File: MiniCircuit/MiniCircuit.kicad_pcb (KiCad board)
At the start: 2 copper layers, 88.8 x 73.9 mm, 32 parts, among them IC1 MAX4737EUD+, IC2 MAX4737EUD+, IC3 MAX4737EUD+, IC4 MAX4737EUD+, J1 Conn_02x16_Odd_Even, J2 Conn_01x08, SW1 SW_DIP_x08, U1 LM6172, U2 OPA2277, U3 MCP3008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

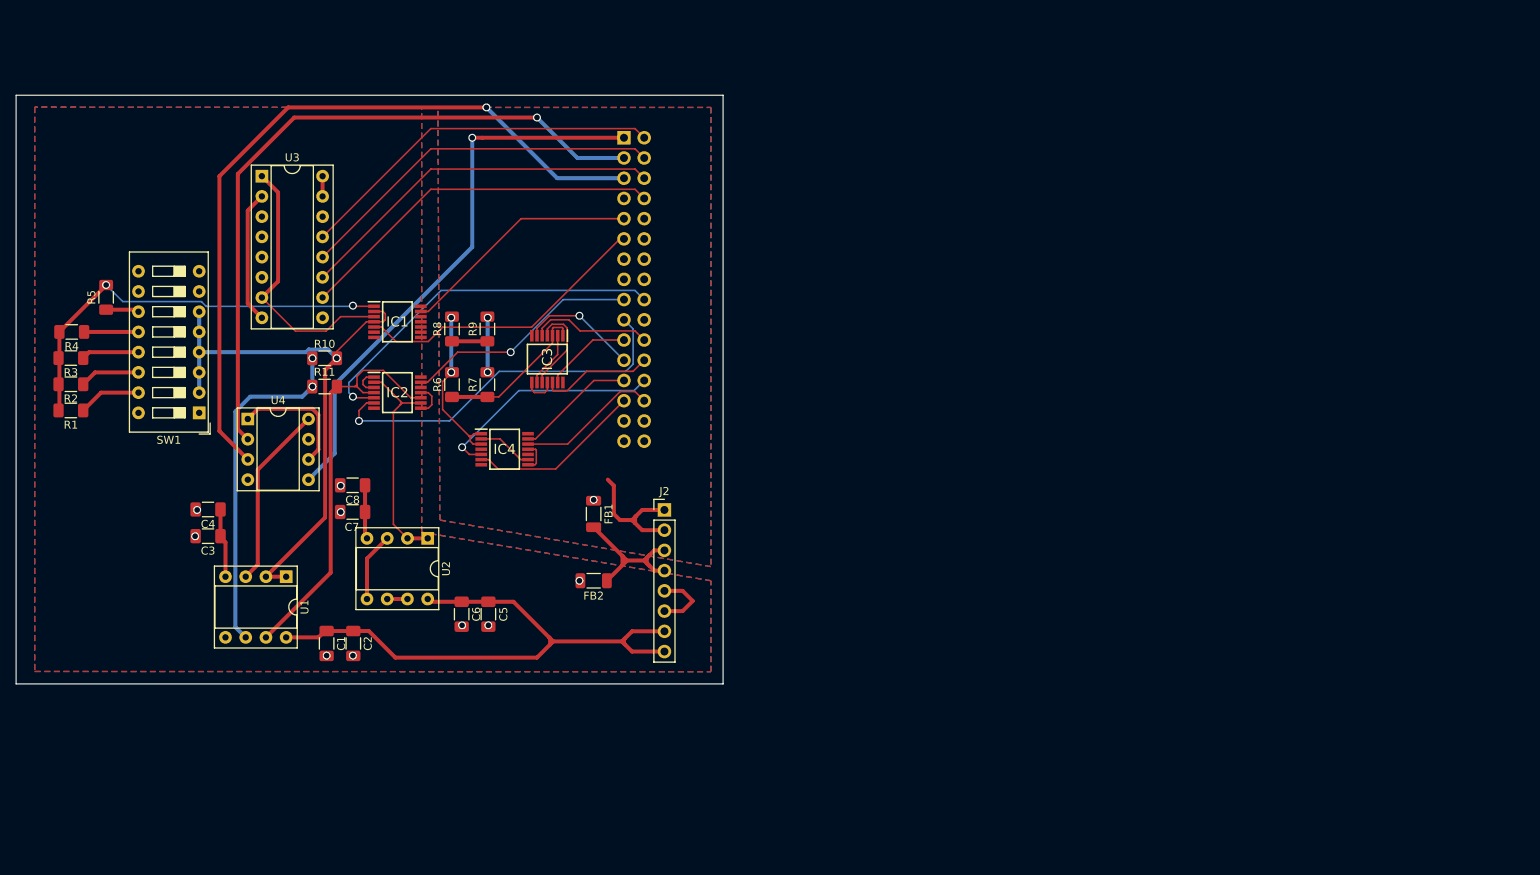
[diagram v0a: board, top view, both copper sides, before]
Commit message: Everything done except routing of digital signals and adding Vias
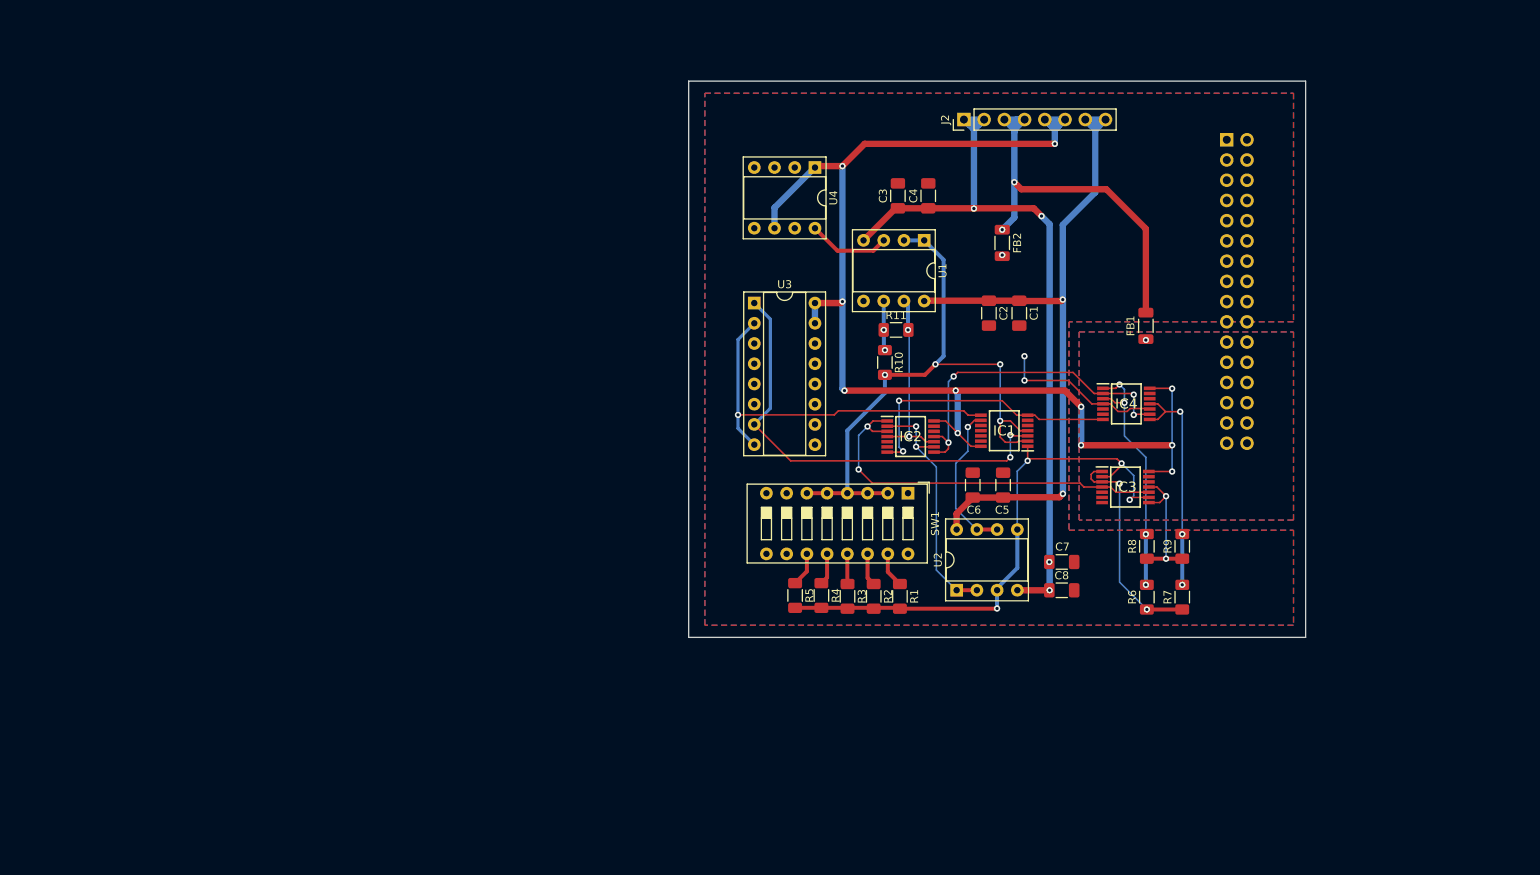
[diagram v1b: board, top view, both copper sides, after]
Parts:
- moved R1 106.7 mm to (161.7, 87.1), turned to -90 degrees
- moved R2 104.3 mm to (158.4, 87.1), turned to -90 degrees
- moved R3 102.0 mm to (155.1, 87.1), turned to -90 degrees
- moved R4 99.8 mm to (151.8, 86.9), turned to -90 degrees
- moved C4 98.6 mm to (165.2, 36.8), turned to 90 degrees
- moved C3 96.6 mm to (161.4, 36.8), turned to 90 degrees
- moved C1 96.4 mm to (176.6, 51.5)
- moved R5 94.3 mm to (148.5, 86.9), turned to -90 degrees
- moved R9 91.4 mm to (197.1, 80.8)
- moved R8 91.4 mm to (192.7, 80.8)
- moved R7 91.2 mm to (197.1, 87.1)
- moved R6 91.2 mm to (192.7, 87.1)
- moved U1 90.6 mm to (164.7, 42.3)
- moved C8 90.0 mm to (182.0, 86.3), turned to 0 degrees
- moved C2 89.9 mm to (172.8, 51.5)
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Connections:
- net /S1in renamed /Driver_FB
- net Net-(U1A-+) renamed /DAC_output
- net Net-(U1B--) renamed /Write_FB
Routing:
- net /+5V: track 26.5 -> 161.1 mm, vias 0 -> 11
- net /SCK: track 95.1 -> 0.00 mm, vias 1 -> 0
- net /DAC_CSbar: track 87.4 -> 0.00 mm, vias 1 -> 0
- net /LDACbar: track 70.5 -> 0.00 mm, vias 1 -> 0
- net /-15V: track 33.3 -> 93.9 mm, vias 0 -> 4
- net /Control10A: track 47.3 -> 0.00 mm, vias 1 -> 0
- net /Control9B: track 47.0 -> 0.00 mm, vias 1 -> 0
- net /Dout: track 46.5 -> 0.00 mm
- net /Din: track 46.5 -> 0.00 mm
- net /ADC_CSbar: track 46.5 -> 0.00 mm
- net /CLK: track 46.5 -> 0.00 mm
- net /Control7: track 37.5 -> 0.00 mm
- net /Write_FB: track 43.4 -> 6.23 mm
- net GNDD: track 0.00 -> 35.2 mm, vias 1 -> 3
- net /S9out: track 15.5 -> 49.0 mm, vias 0 -> 2
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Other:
- board size 88.8 x 73.9 mm -> 77.5 x 69.8 mm

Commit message: Changed Schematic to include CD4066 instead of MAX4737. Design Constraints, Routing and Layout remaining
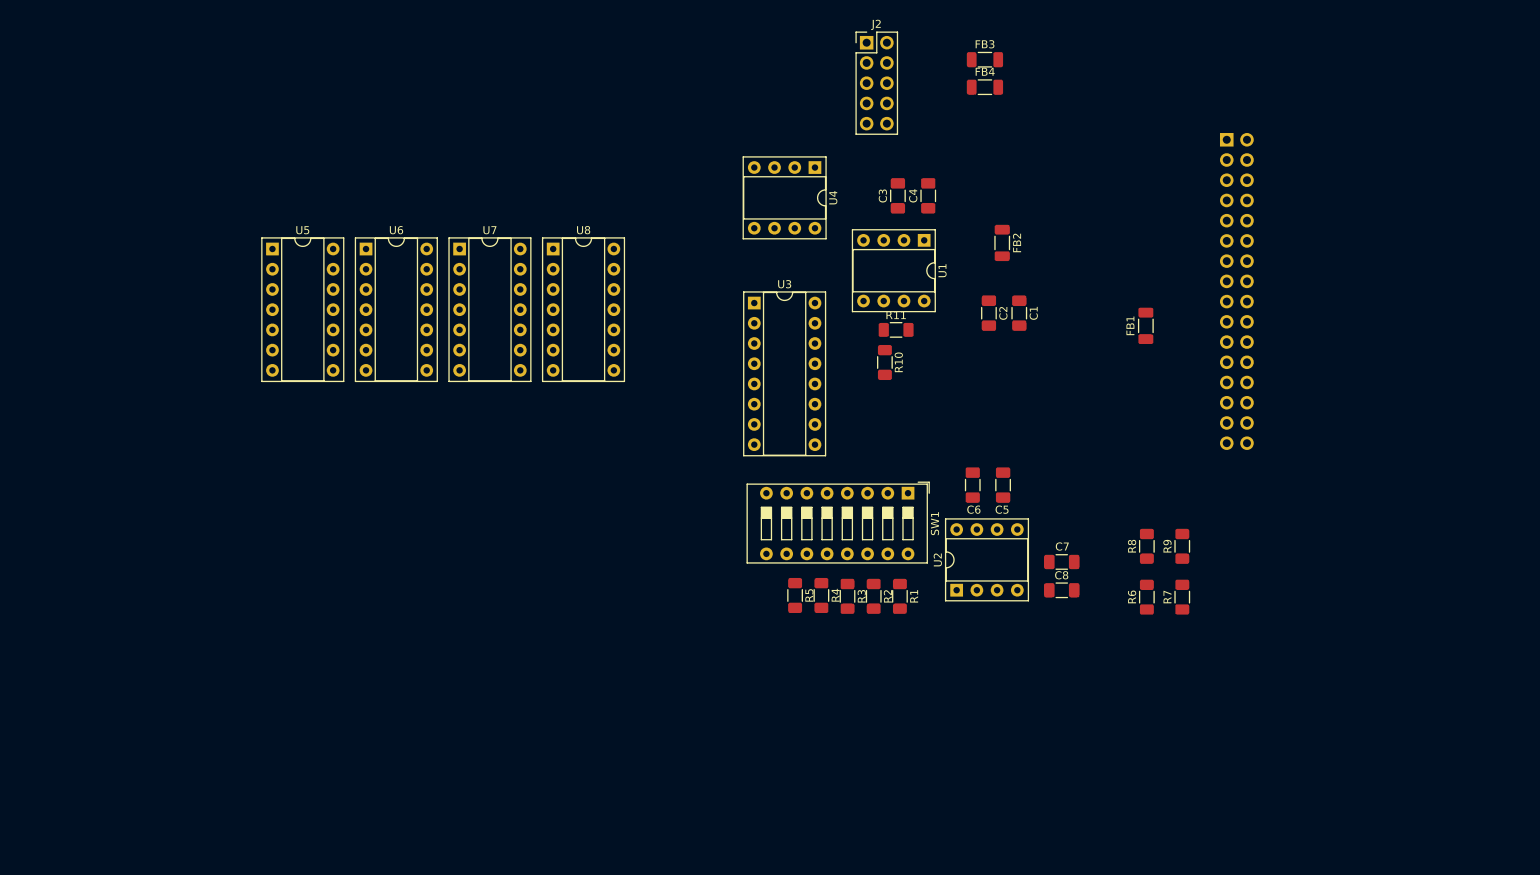
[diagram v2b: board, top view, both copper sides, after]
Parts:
- removed IC1, IC2, IC3, IC4: MAX4737EUD+, MAX4737:SOP65P640X110-14N
- added FB3: FerriteBead, Inductor_SMD:L_1206_3216Metric_Pad1.22x1.90mm_HandSolder, F.Cu at (172.3, 19.7)
- added FB4: FerriteBead, Inductor_SMD:L_1206_3216Metric_Pad1.22x1.90mm_HandSolder, F.Cu at (172.3, 23.1)
- added U5: CD4066BE, Package_DIP:DIP-14_W7.62mm_Socket, F.Cu at (82.9, 43.4)
- added U6: CD4066BE, Package_DIP:DIP-14_W7.62mm_Socket, F.Cu at (94.6, 43.4)
- added U7: CD4066BE, Package_DIP:DIP-14_W7.62mm_Socket, F.Cu at (106.4, 43.4)
- added U8: CD4066BE, Package_DIP:DIP-14_W7.62mm_Socket, F.Cu at (118.1, 43.4)
- J2: value Conn_01x08 -> Conn_02x05_Top_Bottom; footprint Connector_PinHeader_2.54mm:PinHeader_1x08_P2.54mm_Vertical -> Connector_PinHeader_2.54mm:PinHeader_2x05_P2.54mm_Vertical
- moved J2 15.6 mm to (157.5, 17.5), turned to 0 degrees
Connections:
- J2 pad 1: /-15V -> /+15V
- J2 pad 2: /-15V -> /-5V
- J2 pad 3: /PowerGND -> /-5V
- J2 pad 5: /+5V -> /-15V
- J2 pad 6: /+5V -> /+15V
- J2 pad 7: /+15V -> /+5V
- J2 pad 8: /+15V -> /+5V
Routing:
- net /+5V: track 161.1 -> 0.00 mm, vias 11 -> 0
- net /-15V: track 93.9 -> 0.00 mm, vias 4 -> 0
- net /+15V: track 89.5 -> 0.00 mm, vias 2 -> 0
- net /Driver_FB: track 78.4 -> 0.00 mm, vias 4 -> 0
- net /Driver_op: track 70.8 -> 0.00 mm, vias 4 -> 0
- net /S7out: track 56.2 -> 0.00 mm, vias 2 -> 0
- net /PowerGND: track 50.4 -> 0.00 mm, vias 2 -> 0
- net /S9out: track 49.0 -> 0.00 mm, vias 2 -> 0
- net /S8out: track 47.9 -> 0.00 mm, vias 1 -> 0
- net /S10out: track 42.0 -> 0.00 mm, vias 4 -> 0
- net GNDD: track 35.2 -> 0.00 mm, vias 3 -> 0
- net /Vt1: track 31.7 -> 0.00 mm, vias 4 -> 0
- net /S10inA: track 31.1 -> 0.00 mm, vias 2 -> 0
- net /Vt2: track 28.5 -> 0.00 mm, vias 3 -> 0
- net /Hz1: track 27.6 -> 0.00 mm, vias 2 -> 0
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- removed copper zone on B.Cu, net GNDA
- removed copper zone on F.Cu, net GNDA
- removed copper zone on B.Cu, net GNDD
- removed copper zone on F.Cu, net GNDD
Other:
- board outline removed

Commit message: PCB Done, only final touch and verification necessary
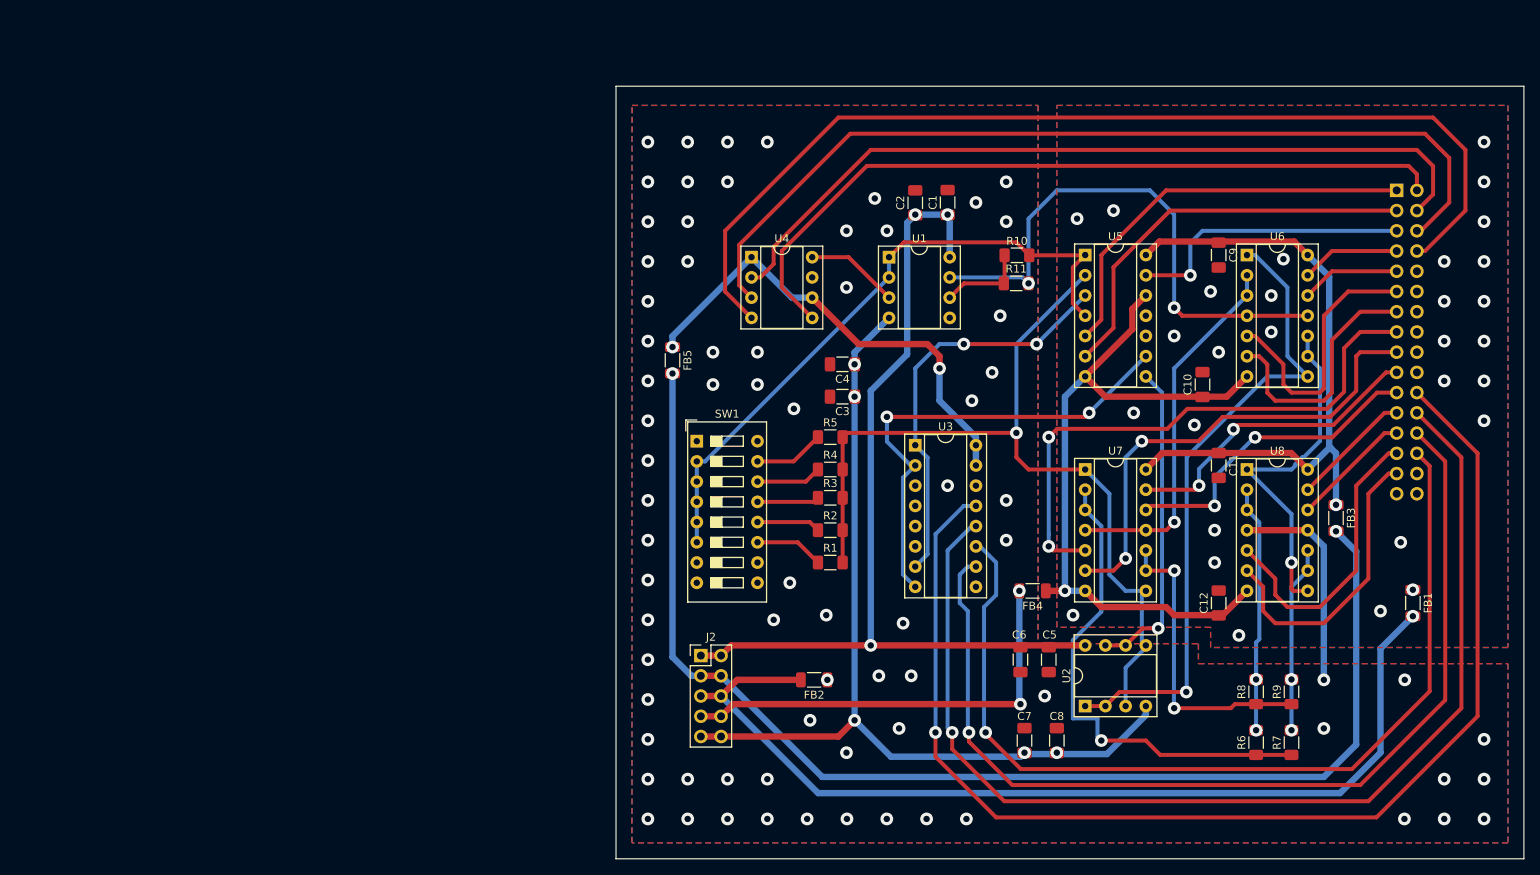
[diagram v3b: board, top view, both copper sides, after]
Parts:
- added C10: 0.1uF, Capacitor_SMD:C_1206_3216Metric_Pad1.33x1.80mm_HandSolder, F.Cu at (199.6, 60.5)
- added C11: 0.1uF, Capacitor_SMD:C_1206_3216Metric_Pad1.33x1.80mm_HandSolder, F.Cu at (201.7, 70.6)
- added C12: 0.1uF, Capacitor_SMD:C_1206_3216Metric_Pad1.33x1.80mm_HandSolder, F.Cu at (201.7, 87.9)
- added C9: 0.1uF, Capacitor_SMD:C_1206_3216Metric_Pad1.33x1.80mm_HandSolder, F.Cu at (201.7, 44.2)
- added FB5: FerriteBead, Inductor_SMD:L_1206_3216Metric_Pad1.22x1.90mm_HandSolder, F.Cu at (133.1, 57.4)
- J2: value Conn_02x05_Top_Bottom -> Conn_02x05_Odd_Even
- moved U6 110.6 mm to (205.2, 44.2)
- moved U5 102.1 mm to (184.9, 44.2)
- moved U8 91.4 mm to (205.2, 71.1)
- moved U7 83.3 mm to (184.9, 71.1)
- moved J2 79.7 mm to (136.7, 94.5)
- moved FB3 72.5 mm to (216.4, 77.2), turned to -90 degrees
- moved FB4 63.5 mm to (178.3, 86.4), turned to 180 degrees
- moved FB2 59.7 mm to (150.9, 97.5), turned to 180 degrees
- moved FB1 48.3 mm to (226.1, 87.9), turned to -90 degrees
- moved SW1 27.3 mm to (136.1, 67.6), turned to 0 degrees
- moved U3 27.0 mm to (163.6, 68.1)
- moved C3 26.2 mm to (154.4, 62.0), turned to 180 degrees
- moved C4 23.7 mm to (154.4, 57.9), turned to 180 degrees
- moved C7 22.9 mm to (177.3, 105.2), turned to 90 degrees
- moved R6 22.8 mm to (206.4, 105.4)
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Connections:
- J1 pad 1: /LDACbar -> /Control7
- J1 pad 11: /Control7 -> /Control9B
- J1 pad 13: /Control8 -> /Control10A
- J1 pad 15: unconnected-(J1-Pin_15-Pad15) -> /ControlAF_1B
- J1 pad 17: /Control9A -> /ControlAF_2A
- J1 pad 18: /Control9B -> unconnected-(J1-Pin_18-Pad18)
- J1 pad 19: /Control10A -> /ControlAF_1A
- J1 pad 2: /CLK -> /LDACbar
- J1 pad 20: /Control10B -> unconnected-(J1-Pin_20-Pad20)
- J1 pad 21: /ControlAF_1A -> /ControlAF_2B
- J1 pad 22: /ControlAF_1B -> /CLK
- J1 pad 23: /ControlAF_2A -> /ControlAF_3A
- J1 pad 24: /ControlAF_2B -> /Dout
- J1 pad 25: /ControlAF_3A -> /ControlAF_4B
- J1 pad 26: /ControlAF_3B -> /ADC_CSbar
- J1 pad 27: /ControlAF_4A -> /ControlAF_3B
- J1 pad 28: /ControlAF_4B -> /Din
- J1 pad 29: unconnected-(J1-Pin_29-Pad29) -> /ControlAF_4A
- J1 pad 3: /DAC_CSbar -> /Control8
- J1 pad 4: /Dout -> /DAC_CSbar
- J1 pad 5: /SCK -> /Control1
- J1 pad 6: /Din -> /SCK
- J1 pad 7: /SDI -> /Control9A
- J1 pad 8: /ADC_CSbar -> /SDI
- J1 pad 9: /Control1 -> /Control10B
- J2 pad 2: /-5V -> /+15V
- J2 pad 3: /-5V -> /+5V
- J2 pad 4: /PowerGND -> /+5V
- J2 pad 5: /-15V -> /PowerGND
- J2 pad 6: /+15V -> /PowerGND
- J2 pad 7: /+5V -> /-5V
- J2 pad 8: /+5V -> /-5V
- J2 pad 9: /PowerGND -> /-15V
- SW1 pad 11: /S6out -> /S2out
- SW1 pad 12: /S5out -> /S3out
- SW1 pad 14: /S3out -> /S5out
- SW1 pad 15: /S2out -> /S6out
- U3 pad 15: /+5V -> /+5VA
- U3 pad 16: /+5V -> /+5VA
- U4 pad 1: /+5V -> /+5VA
- U4 pad 6: /+5V -> /+5VA
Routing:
- net /+5V: track 0.00 -> 157.2 mm, vias 0 -> 2
- net /CLK: track 0.00 -> 154.8 mm, vias 0 -> 1
- net /Dout: track 0.00 -> 140.9 mm, vias 0 -> 1
- net /SDI: track 0.00 -> 128.7 mm
- net /ADC_CSbar: track 0.00 -> 125.4 mm, vias 0 -> 1
- net /PowerGND: track 0.00 -> 122.2 mm, vias 0 -> 1
- net /Din: track 0.00 -> 117.8 mm, vias 0 -> 1
- net /+15V: track 0.00 -> 114.7 mm, vias 0 -> 3
- net /SCK: track 0.00 -> 114.6 mm
- net /-15V: track 0.00 -> 114.5 mm, vias 0 -> 5
- net /Driver_op: track 0.00 -> 109.3 mm, vias 0 -> 1
- net /DAC_CSbar: track 0.00 -> 100.7 mm
- net /LDACbar: track 0.00 -> 96.6 mm
- net /-5VD: track 0.00 -> 91.5 mm, vias 0 -> 1
- net /Driver_FB: track 0.00 -> 81.4 mm
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- added copper zone on B.Cu, net GNDA
- added copper zone on F.Cu, net GNDA
- added copper zone on B.Cu, net GNDD
- added copper zone on F.Cu, net GNDD
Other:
- board outline added: 114 x 97 mm

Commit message: All errors and warnings rectified. Silkscreen contents added.
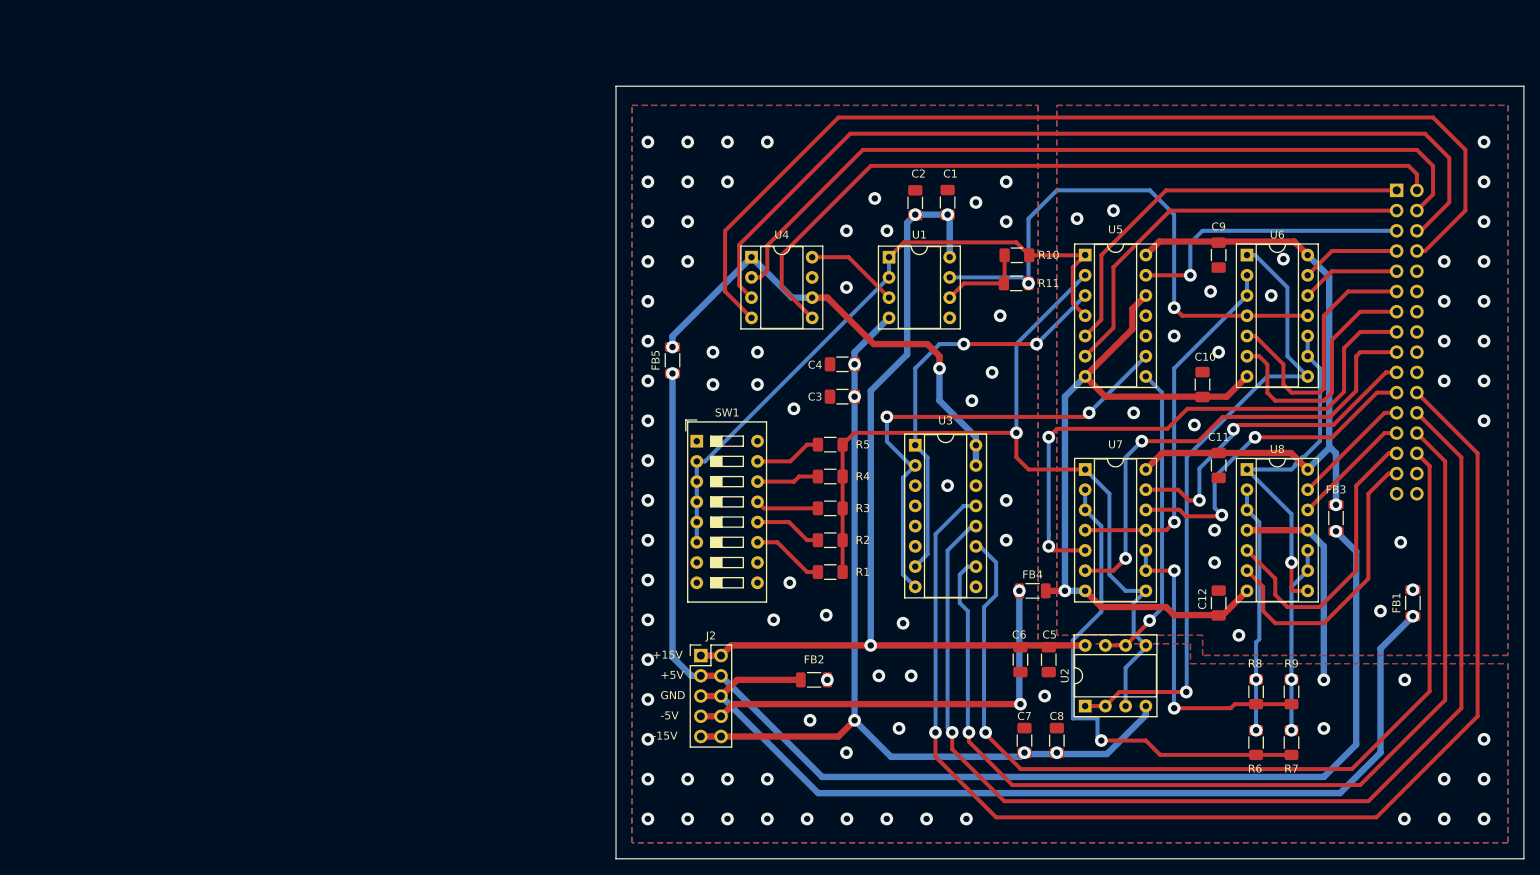
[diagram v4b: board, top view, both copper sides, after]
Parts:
- moved R3 1.32 mm to (152.9, 76.0)
- moved R2 1.26 mm to (152.9, 80.0)
- moved R1 1.20 mm to (152.9, 84.0)
- moved R5 0.94 mm to (152.9, 68.0)
- moved R4 0.88 mm to (152.9, 72.0)
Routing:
- net /Vt1: track 34.6 -> 31.0 mm
- net /ControlAF_2B: track 39.7 -> 42.4 mm
- net /ControlAF_1A: track 39.2 -> 41.4 mm
- net /Driver_op: track 109.3 -> 110.8 mm
- net /S8in: track 40.2 -> 39.1 mm
- net /DAC_CSbar: track 100.7 -> 101.3 mm
- net /S3out: track 8.01 -> 8.54 mm
- net GNDD: vias 28 -> 27
- net (no net): vias 1 -> 0
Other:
- board text added: "+15V"
- board text added: "+5V"
- board text added: "-15V"
- board text added: "-5V"
- board text added: "1"
- board text added: "2"
- board text added: "31 (GND)"
- board text added: "32"
- board text added: "GND"
